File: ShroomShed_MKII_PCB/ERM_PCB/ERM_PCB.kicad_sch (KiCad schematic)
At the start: 16 parts, among them J1 Fan, J2 Humidifier, J3 Conn_01x04, Q1 BSS123, Q2 BSS123

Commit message: got the display working thank fuck
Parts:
- J3: footprint DOWNLOAD_Connectors:CONN_532610001-SD_04_MOL -> Connector_JST:JST_XH_S4B-XH-A-1_1x04_P2.50mm_Horizontal
- L1: DESCRIPTION C3000009 -> (none); P# (none) -> C3000009
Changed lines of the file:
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@@
 			)
 		)
-		(property "DESCRIPTION" "C3000009"
+		(property "P#" "C3000009"
 			(at 196.85 52.07 0)
 			(effects
@@
 			)
 		)
-		(property "Footprint" "DOWNLOAD_Connectors:CONN_532610001-SD_04_MOL"
+		(property "Footprint" "Connector_JST:JST_XH_S4B-XH-A-1_1x04_P2.50mm_Horizontal"
 			(at 203.2 135.255 0)
 			(effects

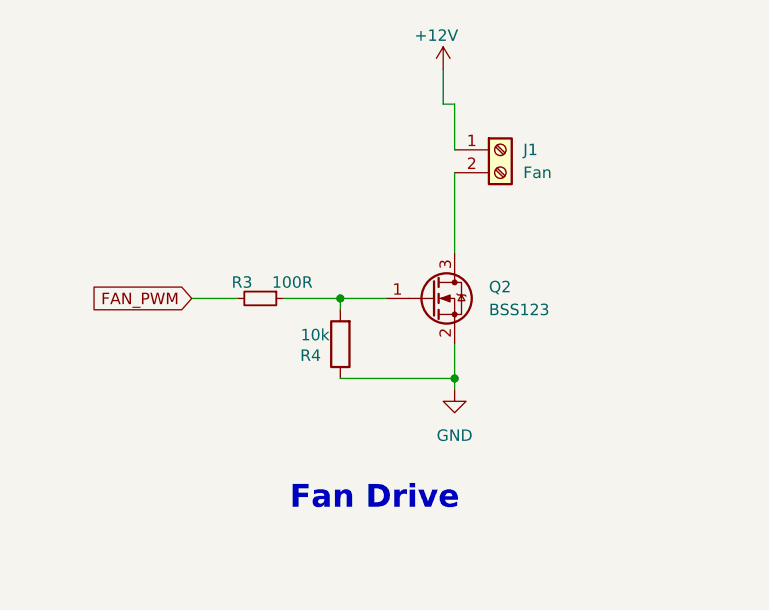
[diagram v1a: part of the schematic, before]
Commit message: completed controler V2.2, got basic blocking implementation of display SPI DMA working
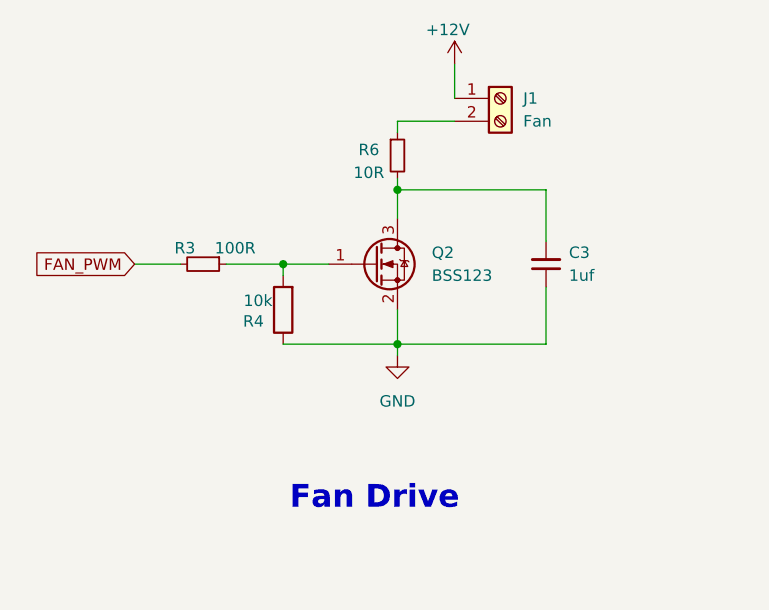
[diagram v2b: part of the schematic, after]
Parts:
- added C3: 1uf, Capacitor_SMD:C_0603_1608Metric, symbol Device:C_Small
- added R6: 10R, Resistor_SMD:R_0805_2012Metric, symbol Device:R_Small
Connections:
- net GND: now also C3.1
- net at J1.2 (Pin_2): now also R6.1; no longer Q2.3 (D)
- new net: C3.2, Q2.3 (D), R6.2
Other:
- moved on the sheet: J1, Q2, R3, R4

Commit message: Controller V2.2 ordered
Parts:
- removed C3: 1uf, Capacitor_SMD:C_0603_1608Metric, symbol Device:C_Small
- removed R6: 10R, Resistor_SMD:R_0805_2012Metric, symbol Device:R_Small
- R1, R3: DESCRIPTION C22775 -> (none)
- R2, R4, R5: DESCRIPTION C25804 -> (none)
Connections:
- net at J1.2 (Pin_2): now also Q2.3 (D)
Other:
- moved on the sheet: J1, Q2, R3, R4
